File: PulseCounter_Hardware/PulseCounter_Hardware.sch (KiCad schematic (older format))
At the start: 34 parts, among them J1 Conn_01x02_Male, Q1 MMBT3904-TP, Q2 MMBT3904-TP, Q3 MMBT3904-TP, Q4 MMBT3904-TP, Q5 MMBT3904-TP, Q6 MMBT3904-TP, U1 LD1117V33, U2 W25Q32JVSSIQ_TR, U3 STM32F103C8Tx

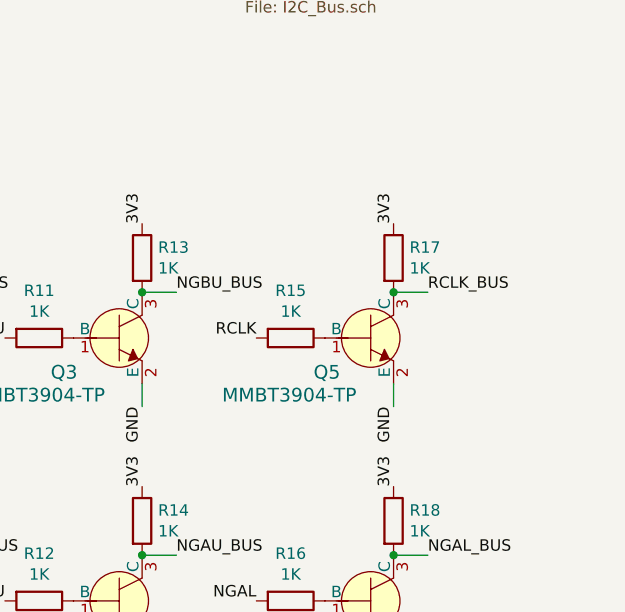
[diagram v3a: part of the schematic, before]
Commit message: Fixed RCLK bus
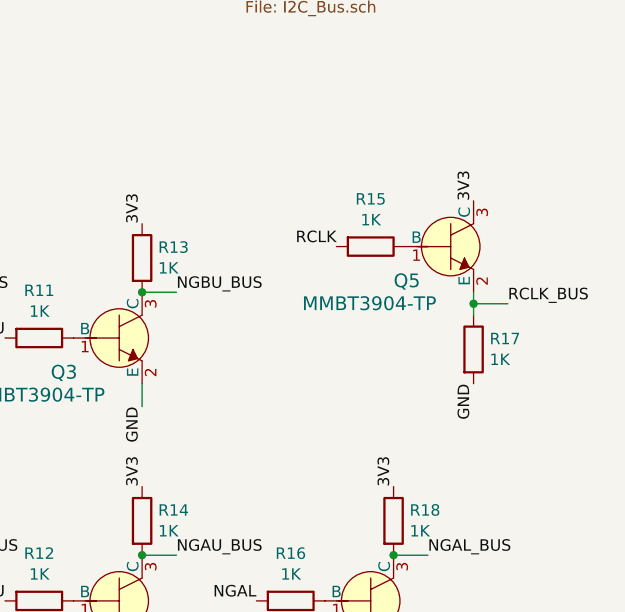
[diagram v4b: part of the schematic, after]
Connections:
- net 3V3: now also Q5.3 (C); no longer R17.1
- net GND: now also R17.2; no longer Q5.2 (E)
- net RCLK_BUS: now also Q5.2 (E), R17.1; no longer Q5.3 (C), R17.2
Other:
- moved on the sheet: Q5, R15, R17
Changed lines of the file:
@@
 Text Label 9100 4150 0    50   ~ 0
 NGBU_BUS
-Text Label 10200 4150 0    50   ~ 0
+Text Label 10550 4200 0    50   ~ 0
 RCLK_BUS
 Text Label 8000 5300 0    50   ~ 0
@@
 Wire Wire Line
 	4050 1450 4050 1600
-Text Label 10050 3850 1    50   ~ 0
+Text Label 10400 3750 1    50   ~ 0
 3V3
 $Comp
 L Device:R R15
 U 1 1 5F74ED3D
-P 9600 4350
-F 0 "R15" V 9393 4350 50  0000 C CNN
-F 1 "1K" V 9484 4350 50  0000 C CNN
-F 2 "Resistor_SMD:R_0603_1608Metric_Pad1.05x0.95mm_HandSolder" V 9530 4350 50  0001 C CNN
-F 3 "~" H 9600 4350 50  0001 C CNN
-	1    9600 4350
+P 9950 3950
+F 0 "R15" V 9743 3950 50  0000 C CNN
+F 1 "1K" V 9834 3950 50  0000 C CNN
+F 2 "Resistor_SMD:R_0603_1608Metric_Pad1.05x0.95mm_HandSolder" V 9880 3950 50  0001 C CNN
+F 3 "~" H 9950 3950 50  0001 C CNN
+	1    9950 3950
 	0    1    1    0
 $EndComp
@@
 L Device:R R17
 U 1 1 5F74ED43
-P 10050 4000
-F 0 "R17" H 10120 4046 50  0000 L CNN
-F 1 "1K" H 10120 3955 50  0000 L CNN
-F 2 "Resistor_SMD:R_0603_1608Metric_Pad1.05x0.95mm_HandSolder" V 9980 4000 50  0001 C CNN
-F 3 "~" H 10050 4000 50  0001 C CNN
-	1    10050 4000
-	1    0    0    -1
-$EndComp
-Wire Wire Line
-	10050 4150 10200 4150
+P 10400 4400
+F 0 "R17" H 10470 4446 50  0000 L CNN
+F 1 "1K" H 10470 4355 50  0000 L CNN
+F 2 "Resistor_SMD:R_0603_1608Metric_Pad1.05x0.95mm_HandSolder" V 10330 4400 50  0001 C CNN
+F 3 "~" H 10400 4400 50  0001 C CNN
+	1    10400 4400
+	1    0    0    -1
+$EndComp
 $Comp
 L dk_Transistors-Bipolar-BJT-Single:MMBT3904-TP Q5
 U 1 1 5F74ED53
-P 9950 4350
-F 0 "Q5" H 9700 4200 60  0000 L CNN
-F 1 "MMBT3904-TP" H 9300 4100 60  0000 L CNN
-F 2 "digikey-footprints:SOT-23-3" H 10150 4550 60  0001 L CNN
-F 3 "https://www.mccsemi.com/pdf/Products/MMBT3904(SOT-23).pdf" H 10150 4650 60  0001 L CNN
-F 4 "MMBT3904TPMSCT-ND" H 10150 4750 60  0001 L CNN "Digi-Key_PN"
-F 5 "MMBT3904-TP" H 10150 4850 60  0001 L CNN "MPN"
-F 6 "Discrete Semiconductor Products" H 10150 4950 60  0001 L CNN "Category"
-F 7 "Transistors - Bipolar (BJT) - Single" H 10150 5050 60  0001 L CNN "Family"
-F 8 "https://www.mccsemi.com/pdf/Products/MMBT3904(SOT-23).pdf" H 10150 5150 60  0001 L CNN "DK_Datasheet_Link"
-F 9 "/product-detail/en/micro-commercial-co/MMBT3904-TP/MMBT3904TPMSCT-ND/717395" H 10150 5250 60  0001 L CNN "DK_Detail_Page"
-F 10 "TRANS NPN 40V 0.2A SOT23" H 10150 5350 60  0001 L CNN "Description"
-F 11 "Micro Commercial Co" H 10150 5450 60  0001 L CNN "Manufacturer"
-F 12 "Active" H 10150 5550 60  0001 L CNN "Status"
-	1    9950 4350
-	1    0    0    -1
-$EndComp
-Connection ~ 10050 4150
-Text Label 10050 4650 3    50   ~ 0
-GND
-Wire Wire Line
-	10050 4650 10050 4550
+P 10300 3950
+F 0 "Q5" H 10050 3800 60  0000 L CNN
+F 1 "MMBT3904-TP" H 9650 3700 60  0000 L CNN
+F 2 "digikey-footprints:SOT-23-3" H 10500 4150 60  0001 L CNN
+F 3 "https://www.mccsemi.com/pdf/Products/MMBT3904(SOT-23).pdf" H 10500 4250 60  0001 L CNN
+F 4 "MMBT3904TPMSCT-ND" H 10500 4350 60  0001 L CNN "Digi-Key_PN"
+F 5 "MMBT3904-TP" H 10500 4450 60  0001 L CNN "MPN"
+F 6 "Discrete Semiconductor Products" H 10500 4550 60  0001 L CNN "Category"
+F 7 "Transistors - Bipolar (BJT) - Single" H 10500 4650 60  0001 L CNN "Family"
+F 8 "https://www.mccsemi.com/pdf/Products/MMBT3904(SOT-23).pdf" H 10500 4750 60  0001 L CNN "DK_Datasheet_Link"
+F 9 "/product-detail/en/micro-commercial-co/MMBT3904-TP/MMBT3904TPMSCT-ND/717395" H 10500 4850 60  0001 L CNN "DK_Detail_Page"
+F 10 "TRANS NPN 40V 0.2A SOT23" H 10500 4950 60  0001 L CNN "Description"
+F 11 "Micro Commercial Co" H 10500 5050 60  0001 L CNN "Manufacturer"
+F 12 "Active" H 10500 5150 60  0001 L CNN "Status"
+	1    10300 3950
+	1    0    0    -1
+$EndComp
+Text Label 10400 4550 3    50   ~ 0
+GND
+Wire Wire Line
+	10400 4250 10400 4200
 Text Label 8950 5000 1    50   ~ 0
 3V3
@@
 Text Label 8000 4150 0    50   ~ 0
 NGBL_BUS
-Text Label 9450 4350 2    50   ~ 0
+Text Label 9800 3950 2    50   ~ 0
 RCLK
 Text Label 7250 5500 2    50   ~ 0
@@
 Wire Wire Line
 	4350 1300 4800 1300
+Wire Wire Line
+	10400 4200 10550 4200
+Connection ~ 10400 4200
+Wire Wire Line
+	10400 4200 10400 4150
 $EndSCHEMATC
